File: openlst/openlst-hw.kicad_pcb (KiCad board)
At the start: 4 copper layers, 51.7 x 29.2 mm, 73 parts, among them J10 Conn_01x02, J2 CC Prog/Debug, J3 UART0, J4 SPI0, J5 Control Outputs, J6 ANT, J9 Conn_01x02, U2 CC1110, U4 FOX924 27MHz, U5 TLV803S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

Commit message: Finalized BOM
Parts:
- removed C31: 0.1u, Capacitor_SMD:C_0603_1608Metric
- removed J10, J9: Conn_01x02, Connector_PinHeader_2.54mm:PinHeader_1x02_P2.54mm_Vertical
- removed TP1, TP2, TP3, TP4: TestPoint, TestPoint:TestPoint_Keystone_5010-5014_Multipurpose
- removed TP5: TestPoint, TestPoint:TestPoint_Pad_D1.0mm
- added C12: 0.1u, Capacitor_SMD:C_0603_1608Metric, F.Cu at (128.7, 85.0)
- added C13: 0.01u, Capacitor_SMD:C_0603_1608Metric, F.Cu at (122.6, 90.5)
- added C14: 6.8n, Capacitor_SMD:C_0603_1608Metric, F.Cu at (126.6, 90.5)
- added C15: 22u, Capacitor_SMD:C_1210_3225Metric, F.Cu at (118.2, 85.9)
- added C16: 22u, Capacitor_SMD:C_1210_3225Metric, F.Cu at (101.8, 96.2)
- added C17: 10u, Capacitor_SMD:C_0805_2012Metric, F.Cu at (111.3, 97.1)
- added C18: 10u, Capacitor_SMD:C_0805_2012Metric, F.Cu at (106.9, 97.1)
- added C4: 10u, Capacitor_SMD:C_0805_2012Metric, F.Cu at (137.3, 77.3)
- added H1: M3 Hole, MountingHole:MountingHole_3.2mm_M3, F.Cu at (115.2, 79.8)
- added H2: M3 Hole, MountingHole:MountingHole_3.2mm_M3, F.Cu at (111.4, 91.6)
- added H3: M3 Hole, MountingHole:MountingHole_3.2mm_M3, F.Cu at (131.1, 79.8)
- added H4: M3 Hole, MountingHole:MountingHole_3.2mm_M3, F.Cu at (123.2, 79.8)
- added J1: Battery, TerminalBlock_Phoenix:TerminalBlock_Phoenix_MKDS-1,5-2-5.08_1x02_P5.08mm_Horizontal, F.Cu at (102.6, 82.0)
- added L1: 10u, Inductor_SMD:L_Vishay_IFSC-1515AH_4x4x1.8mm, F.Cu at (123.9, 86.5)
- added L2: Z=1k @ 100M, Inductor_SMD:L_0603_1608Metric, F.Cu at (115.6, 96.9)
- added R15: 6k8, Resistor_SMD:R_0603_1608Metric, F.Cu at (117.4, 93.7)
- added R19: 36k, Resistor_SMD:R_0603_1608Metric, F.Cu at (137.1, 80.1)
- added R20: 10k, Resistor_SMD:R_0603_1608Metric, F.Cu at (113.2, 85.0)
- added U1: LP2981-3.3, Package_TO_SOT_SMD:SOT-23-5, F.Cu at (118.0, 90.2)
- added U3: AP6502, Package_SO:SOIC-8-1EP_3.9x4.9mm_P1.27mm_EP2.62x3.51mm_ThermalVias, F.Cu at (103.2, 90.9)
- C27: value 0.1u -> 0.01u
- C6: value 0.1u -> 0.22u
- R1, R18, R2, R26, R28, R3, R4: value 1K -> 1k
- R16: value 56K -> 56k
- R21, R27: value 33K -> 33k
- R22: value 10K -> 10k
- R36: value 5K6 -> 6k8
- R37: value 3K3 -> 1k5
- U4: value FOX924 27MHz -> ASFL1-27.000MHZ; footprint Oscillator:Oscillator_SMD_Fordahl_DFAS15-4Pin_5.0x3.2mm -> Oscillator:Oscillator_SMD_SeikoEpson_SG8002LB-4Pin_5.0x3.2mm
- U5: value TLV803S -> MIC803
- U6: value PE4259 -> PE4250; footprint Package_TO_SOT_SMD:SOT-363_SC-70-6 -> Package_SO:MSOP-8_3x3mm_P0.65mm
- U9: value RFFM6406 -> RFFM6404
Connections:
- net /PA_VAPC renamed Net-(C6-Pad1)
- net /~LST_RESET renamed /~{LST_RESET}
- C11 pad 1: VAA -> Net-(C11-Pad1)
- C44 pad 1: VAA -> Net-(C11-Pad1)
- C46 pad 1: VAA -> Net-(C11-Pad1)
- C8 pad 1: VAA -> Net-(C11-Pad1)
- R1 pad 1: +3V3 -> /LST_TX_MODE
- R1 pad 2: /~LST_RX_MODE -> +3V3
- R14 pad 1: /~LST_RX_MODE -> /~{LST_RX_MODE}
- R2 pad 1: /LST_TX_MODE -> /~{LST_RX_MODE}
- U2 pad 32: /~LST_RX_MODE -> /~{LST_RX_MODE}
- U6 pad 1: Net-(C39-Pad1) -> Net-(C26-Pad1)
- U6 pad 2: GND -> /~{LST_RX_MODE}
- U6 pad 3: Net-(C38-Pad1) -> Net-(C25-Pad2)
- U6 pad 4: /~LST_RX_MODE -> GND
- U6 pad 5: Net-(C25-Pad2) -> Net-(C39-Pad1)
- U6 pad 6: Net-(C26-Pad1) -> GND
- U9 pad 14: unconnected-(U9-Pad14) -> GND
- U9 pad 16: unconnected-(U9-Pad16) -> GND
- U9 pad 17: VAA -> Net-(C11-Pad1)
- U9 pad 23: VAA -> GND
- U9 pad 24: VAA -> GND
- U9 pad 25: unconnected-(U9-Pad25) -> GND
- U9 pad 26: VAA -> Net-(C11-Pad1)
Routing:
- net VAA: track 22.4 -> 0.00 mm, vias 3 -> 0
- net Net-(C11-Pad1): track 0.00 -> 22.4 mm, vias 0 -> 3
- net /~{LST_RX_MODE}: track 0.00 -> 22.2 mm, vias 0 -> 2
- net /~LST_RX_MODE: track 22.2 -> 0.00 mm, vias 2 -> 0
- net Net-(C26-Pad1): track 3.37 -> 7.19 mm
- net Net-(C25-Pad2): track 2.49 -> 0.00 mm
- net GND: track 1.27 -> 3.76 mm
- net Net-(C38-Pad1): track 1.92 -> 0.00 mm
- net Net-(C39-Pad1): track 1.90 -> 0.00 mm
- net /LST_TX_MODE: track 41.2 -> 42.2 mm, vias 3 -> 4
- net +3V3: track 25.2 -> 24.3 mm, vias 7 -> 6

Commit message: Started OpenLST PCB
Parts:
- U3: footprint Package_SO:SOIC-8-1EP_3.9x4.9mm_P1.27mm_EP2.62x3.51mm_ThermalVias -> openlst:SOIC-8-1EP_3.9x4.9mm_P1.27mm_EP2.613x3.502mm
- moved H2 75.2 mm to (183.8, 111.9)
- moved C16 71.4 mm to (172.8, 103.9), turned to 90 degrees
- moved U3 63.8 mm to (164.3, 109.4), turned to 90 degrees
- moved L2 63.3 mm to (178.8, 100.4), turned to 90 degrees
- moved J1 55.0 mm to (149.8, 110.2)
- moved R20 54.8 mm to (164.8, 103.4), turned to 90 degrees
- moved C13 54.3 mm to (172.3, 112.4), turned to 180 degrees
- moved C15 54.2 mm to (169.3, 103.9), turned to 90 degrees
- moved H3 53.8 mm to (183.8, 68.9)
- moved C10 53.7 mm to (151.6, 41.5)
- moved C19 53.7 mm to (149.9, 41.5)
- moved C2 53.7 mm to (152.6, 44.5)
- moved C21 53.7 mm to (155.3, 50.5)
- moved C22 53.7 mm to (151.5, 36.3)
- moved C24 53.7 mm to (155.9, 48.5)
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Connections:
- net Net-(C11-Pad1) renamed /VAA_FILT
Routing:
- net /~{LST_RESET}: track 51.8 -> 0.00 mm, vias 2 -> 0
- net /LST_TX_MODE: track 42.2 -> 0.00 mm, vias 4 -> 0
- net /RF_BYP: track 38.6 -> 0.00 mm, vias 3 -> 0
- net /RF_EN: track 33.3 -> 0.00 mm, vias 3 -> 0
- net +BATT: track 0.00 -> 29.6 mm, vias 0 -> 4
- net /3V3_FILT: track 22.5 -> 0.00 mm, vias 7 -> 0
- net /VAA_FILT: track 22.4 -> 0.00 mm, vias 3 -> 0
- net /~{LST_RX_MODE}: track 22.2 -> 0.00 mm, vias 2 -> 0
- net +3V3: track 24.3 -> 2.36 mm, vias 6 -> 0
- net /AN0: track 21.6 -> 0.00 mm, vias 2 -> 0
- net /PROG_DC: track 14.1 -> 0.00 mm, vias 2 -> 0
- net Net-(C13-Pad1): track 0.00 -> 13.7 mm, vias 0 -> 2
- net /UART0_CTS: track 12.6 -> 0.00 mm
- net Net-(C22-Pad1): track 12.3 -> 0.00 mm, vias 2 -> 0
- net /PROG_DD: track 11.8 -> 0.00 mm, vias 2 -> 0
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- added copper zone on F.Cu, net +BATT
- added copper zone on F.Cu, net Net-(C13-Pad2)
- added copper zone on F.Cu, net VAA
- removed copper zone on In2.Cu, net +3V3
- removed copper zone on In2.Cu, net /3V3_FILT
- removed copper zone on B.Cu, net GND
- removed copper zone on In2.Cu, net VAA
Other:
- board size 51.7 x 29.2 mm -> 50 x 50 mm
- board text added: "BATT"
- board text removed: "3V3"
- board text removed: "VAA"

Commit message: Finished OpenLST PCB
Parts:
- moved R21 61.6 mm to (175.6, 104.4), turned to -90 degrees
- moved R22 60.0 mm to (175.6, 101.2), turned to -90 degrees
- moved R27 59.7 mm to (162.8, 99.9), turned to -90 degrees
- moved R18 58.5 mm to (162.8, 96.9), turned to -90 degrees
- moved U5 57.6 mm to (161.8, 93.4)
- moved C22 57.6 mm to (158.8, 93.4)
- moved C2 48.5 mm to (155.3, 92.9), turned to -90 degrees
- moved R26 47.5 mm to (179.8, 94.7), turned to 0 degrees
- moved J3 46.1 mm to (159.9, 75.4), turned to -90 degrees
- moved R28 45.1 mm to (179.8, 92.7), turned to 0 degrees
- moved C9 45.1 mm to (149.3, 97.9), turned to 90 degrees
- moved C47 45.0 mm to (147.3, 97.9), turned to 90 degrees
- moved R17 44.1 mm to (155.8, 95.9)
- moved C27 44.0 mm to (155.8, 99.4), turned to 90 degrees
- moved D1 43.5 mm to (151.8, 96.7), turned to 90 degrees
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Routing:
- net GND: track 3.05 -> 99.4 mm, vias 0 -> 94
- net /RF_EN: track 0.00 -> 41.4 mm, vias 0 -> 2
- net /RF_BYP: track 0.00 -> 40.5 mm, vias 0 -> 2
- net /AN0: track 0.00 -> 39.8 mm, vias 0 -> 2
- net /LST_TX_MODE: track 0.00 -> 33.3 mm, vias 0 -> 3
- net /3V3_FILT: track 0.00 -> 32.1 mm, vias 0 -> 6
- net Net-(C22-Pad1): track 0.00 -> 28.5 mm, vias 0 -> 2
- net +3V3: track 2.36 -> 27.7 mm, vias 0 -> 8
- net /PROG_DD: track 0.00 -> 23.8 mm, vias 0 -> 2
- net /~{LST_RX_MODE}: track 0.00 -> 21.8 mm, vias 0 -> 2
- net /UART0_RTS: track 0.00 -> 16.4 mm
- net /PROG_DC: track 0.00 -> 15.3 mm, vias 0 -> 2
- net /VAA_FILT: track 0.00 -> 11.4 mm, vias 0 -> 2
- net /UART0_TX: track 0.00 -> 11.3 mm
- net Net-(R16-Pad2): track 0.00 -> 8.35 mm, vias 0 -> 2
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- added copper zone on In2.Cu, net +3V3
- added copper zone on In2.Cu, net /3V3_FILT
- added copper zone on In2.Cu, net /VAA_FILT
- added copper zone on In2.Cu, net VAA
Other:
- board size 50 x 50 mm -> 50 x 43 mm
- board text added: "CS"
- board text added: "CTS"
- board text added: "LST_RX"
- board text added: "LST_TX"
- board text added: "MISO"
- board text added: "MOSI"
- board text added: "OpenLST v2.5 Copyright 2018 Planet Labs Inc Copyright 2021 Nathan Kerns"
- board text added: "RTS"
- board text added: "RX"
- board text added: "SCK"
- board text added: "TX"

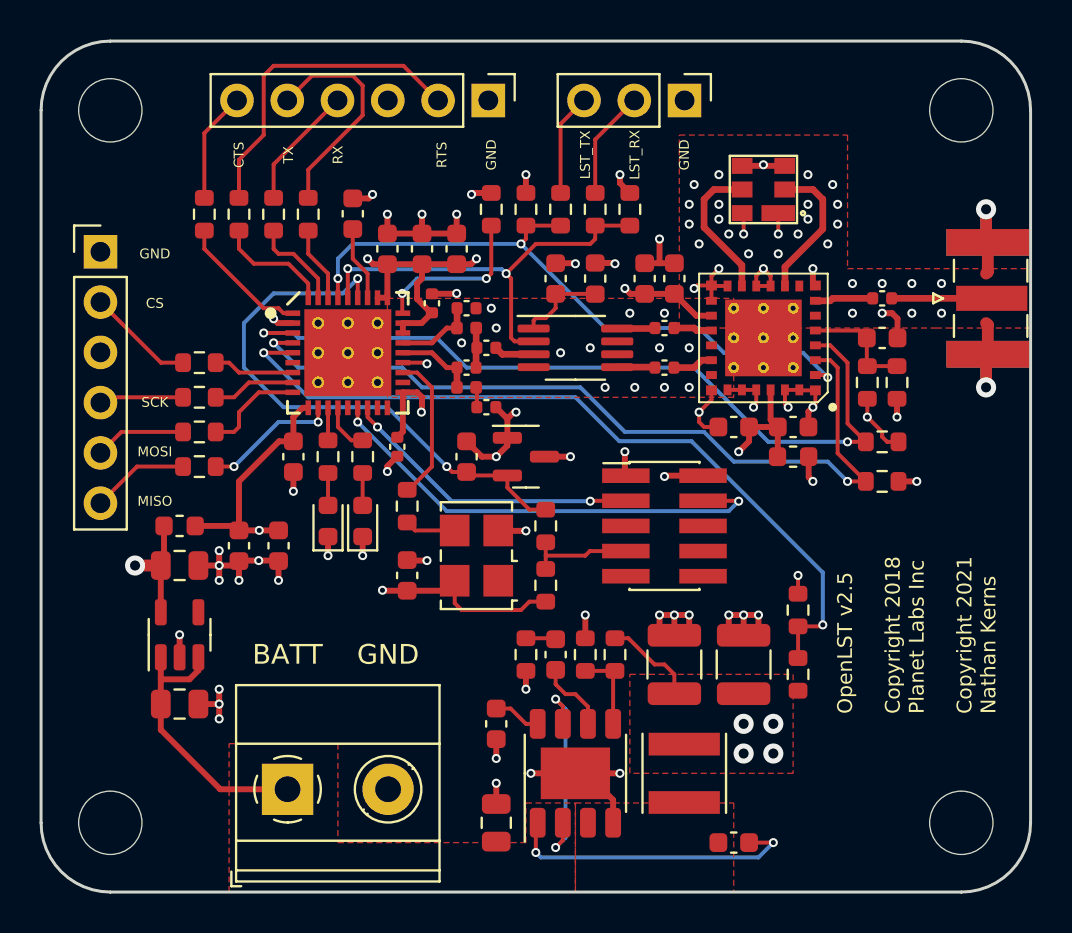
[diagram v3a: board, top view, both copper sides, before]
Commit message: Finals checks of PCB and gerber generation
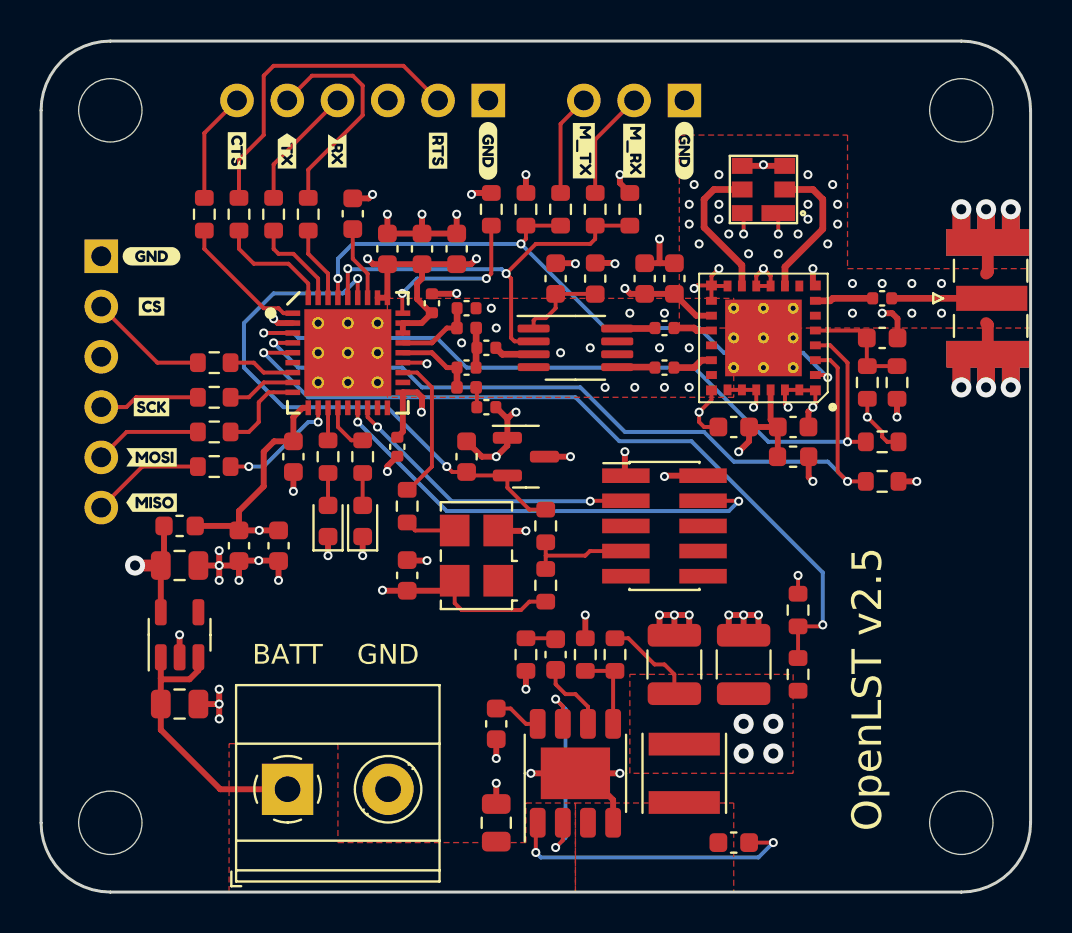
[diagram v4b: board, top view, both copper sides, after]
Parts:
- added kibuzzard-610AE595: G***, kibuzzard-610AE595, F.Cu at (147.2, 77.9)
- added kibuzzard-610AE658: G***, kibuzzard-610AE658, F.Cu at (157.4, 77.9)
- added kibuzzard-610AE73D: G***, kibuzzard-610AE73D, F.Cu at (159.9, 78.0)
- added kibuzzard-610AE73D: G***, kibuzzard-610AE73D, F.Cu at (169.8, 77.9)
- added kibuzzard-610AE73D: G***, kibuzzard-610AE73D, F.Cu at (142.9, 83.3)
- added kibuzzard-610AE761: G***, kibuzzard-610AE761, F.Cu at (149.7, 78.0)
- added kibuzzard-610AE773: G***, kibuzzard-610AE773, F.Cu at (152.3, 78.0)
- added kibuzzard-610AE8D4: G***, kibuzzard-610AE8D4, F.Cu at (142.9, 85.8)
- added kibuzzard-610AE8E6: G***, kibuzzard-610AE8E6, F.Cu at (142.9, 90.9)
- added kibuzzard-610AE965: G***, kibuzzard-610AE965, F.Cu at (142.9, 93.4)
- added kibuzzard-610AE972: G***, kibuzzard-610AE972, F.Cu at (142.9, 95.7)
- added kibuzzard-610AE9EB: G***, kibuzzard-610AE9EB, F.Cu at (167.3, 77.9)
- added kibuzzard-610AEA01: G***, kibuzzard-610AEA01, F.Cu at (164.7, 77.9)
- moved R5 0.75 mm to (146.1, 88.7)
- moved R6 0.75 mm to (146.1, 90.4)
- moved R7 0.75 mm to (146.1, 92.2)
- moved R8 0.75 mm to (146.1, 93.9)
- moved J4 0.23 mm to (140.3, 83.3)
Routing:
- net GND: track 99.4 -> 107.5 mm, vias 94 -> 98
- net +3V3: track 27.7 -> 26.8 mm
- net /CAN_MOSI: track 4.61 -> 5.41 mm
- net /CAN_MISO: track 4.94 -> 5.74 mm
- net /CAN_SCK: track 4.29 -> 5.09 mm
- net Net-(R5-Pad1): track 4.10 -> 3.35 mm
- net Net-(R8-Pad1): track 6.83 -> 6.08 mm
- net Net-(R6-Pad1): track 4.21 -> 3.46 mm
- net /CAN_CS: track 5.44 -> 6.06 mm
- net Net-(R7-Pad1): track 5.16 -> 4.56 mm
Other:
- rule pad_to_mask_clearance: 0.0762 -> 0.0381
- board text added: "OpenLST v2.5"
- board text removed: "CS"
- board text removed: "CTS"
- board text removed: "LST_RX"
- board text removed: "LST_TX"
- board text removed: "MISO"
- board text removed: "MOSI"
- board text removed: "OpenLST v2.5 Copyright 2018 Planet Labs Inc Copyright 2021 Nathan Kerns"
- board text removed: "RTS"
- board text removed: "RX"
- board text removed: "SCK"
- board text removed: "TX"
